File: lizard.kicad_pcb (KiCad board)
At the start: 2 copper layers, 14.8 x 56.2 mm, 13 parts, among them P1 SW DBG, U1 EFM8BB1

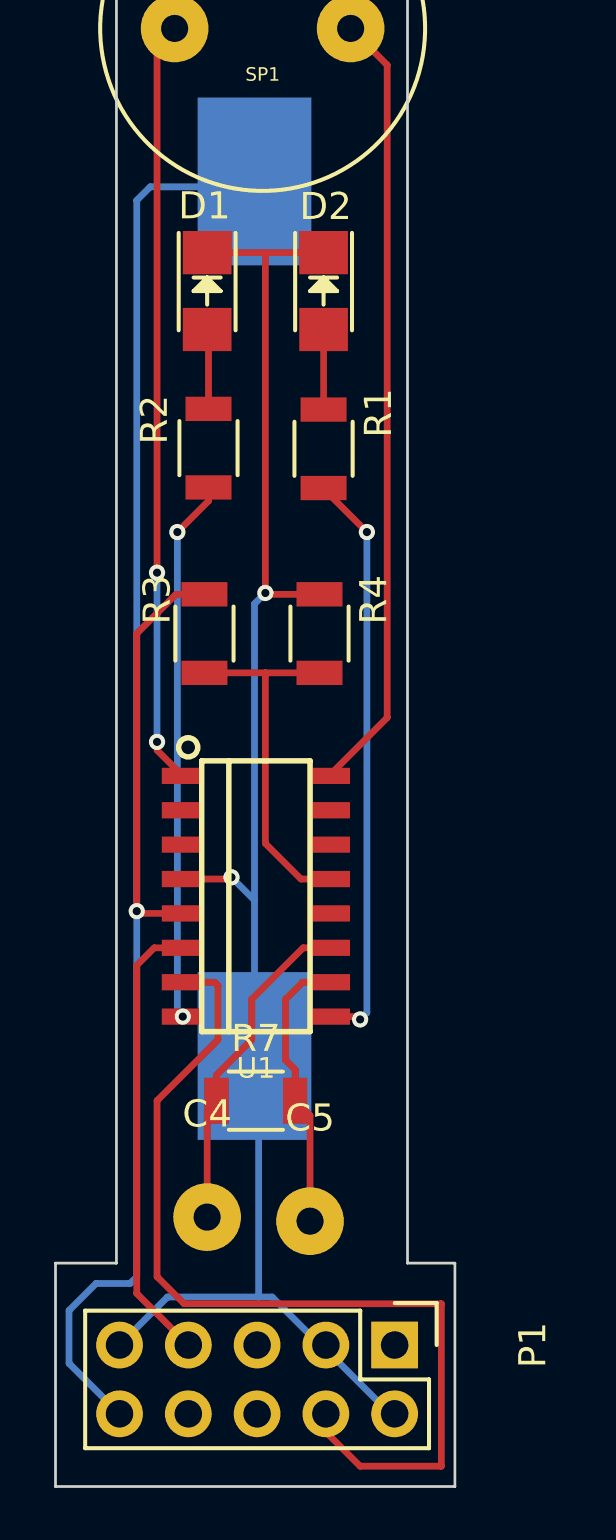
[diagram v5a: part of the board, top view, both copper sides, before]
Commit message: fixed LED resistor values; fixed silk values; misc fixes
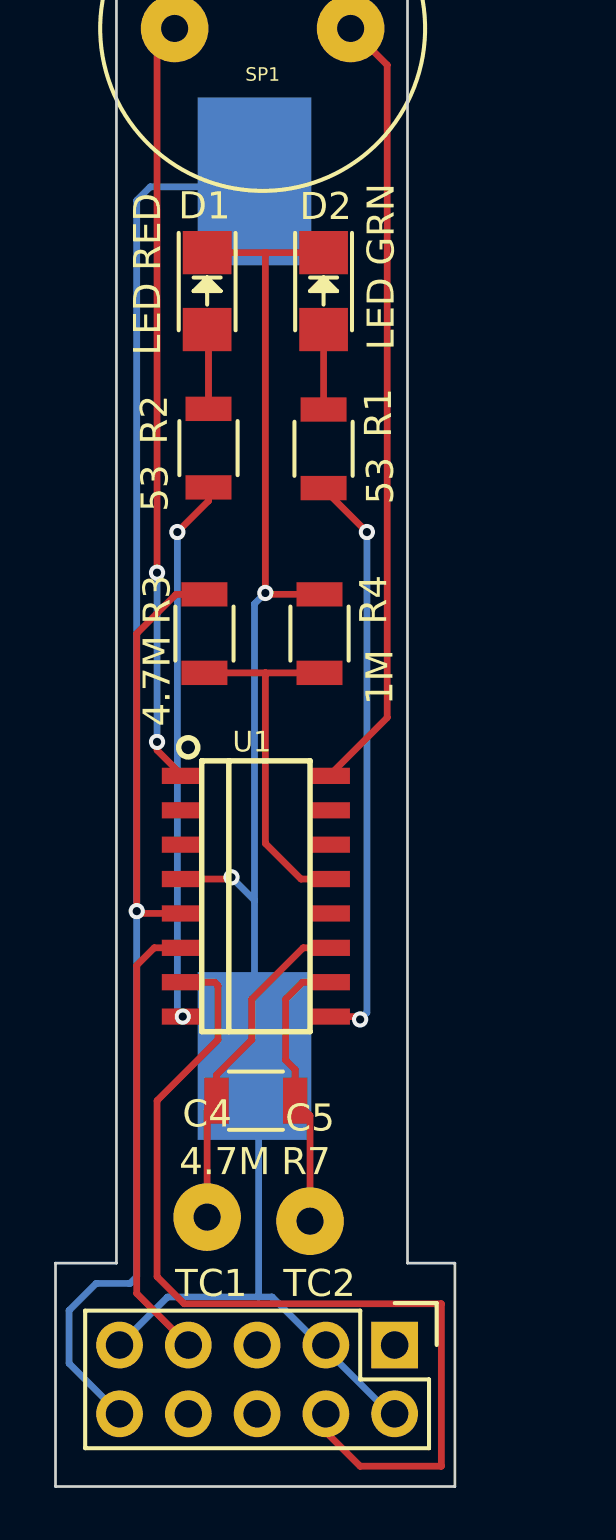
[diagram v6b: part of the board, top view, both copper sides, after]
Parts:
- R1, R2: value 20 -> 53
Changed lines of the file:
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@@
-(kicad_pcb (version 4) (host pcbnew "(2015-06-09 BZR 5726)-product")
+(kicad_pcb (version 4) (host pcbnew "(2015-08-06 BZR 6058)-product")
   (general
     (links 24)
@@
       (effects (font (size 1 1) (thickness 0.15)))
     )
-    (fp_text value TC1 (at -1.905 3.175) (layer F.Fab)
+    (fp_text value TC1 (at 0.15 2.45) (layer F.SilkS)
       (effects (font (size 1 1) (thickness 0.15)))
     )
@@
       (effects (font (size 1 1) (thickness 0.15)))
     )
-    (fp_text value TC2 (at -1.905 3.175) (layer F.Fab)
+    (fp_text value TC2 (at 0.35 2.3) (layer F.SilkS)
       (effects (font (size 1 1) (thickness 0.15)))
     )
@@
       (effects (font (size 1 1) (thickness 0.15)))
     )
-    (fp_text value "LED RED" (at -0.625 2.2 270) (layer F.Fab)
+    (fp_text value "LED RED" (at -0.625 2.2 270) (layer F.SilkS)
       (effects (font (size 1 1) (thickness 0.15)))
     )
@@
       (effects (font (size 1 1) (thickness 0.15)))
     )
-    (fp_text value "LED GRN" (at -0.9 -2.125 270) (layer F.Fab)
+    (fp_text value "LED GRN" (at -0.9 -2.125 270) (layer F.SilkS)
       (effects (font (size 1 1) (thickness 0.15)))
     )
@@
     (descr "Through hole pin header")
     (tags "pin header")
-    (fp_text reference P1 (at 0 -5.1 270) (layer F.SilkS)
-      (effects (font (size 1 1) (thickness 0.15)))
-    )
-    (fp_text value "SW DBG" (at 0 -3.1 270) (layer F.Fab)
+    (fp_text reference P1 (at 0 -5.1 270) (layer F.SilkS) hide
+      (effects (font (size 1 1) (thickness 0.15)))
+    )
+    (fp_text value "SW DBG" (at 0 -3.1 270) (layer F.SilkS) hide
       (effects (font (size 1 1) (thickness 0.15)))
     )
@@
       (effects (font (size 1 1) (thickness 0.15)))
     )
-    (fp_text value 20 (at 1.175 -2.1 270) (layer F.Fab)
+    (fp_text value 53 (at 1.175 -2.1 270) (layer F.SilkS)
       (effects (font (size 1 1) (thickness 0.15)))
     )
@@
       (effects (font (size 1 1) (thickness 0.15)))
     )
-    (fp_text value 20 (at 1.475 1.975 270) (layer F.Fab)
+    (fp_text value 53 (at 1.475 1.975 270) (layer F.SilkS)
       (effects (font (size 1 1) (thickness 0.15)))
     )
@@
       (effects (font (size 1 1) (thickness 0.15)))
     )
-    (fp_text value 4.7M (at 1.75 1.75 270) (layer F.Fab)
+    (fp_text value 4.7M (at 1.75 1.75 270) (layer F.SilkS)
       (effects (font (size 1 1) (thickness 0.15)))
     )
@@
       (effects (font (size 1 1) (thickness 0.15)))
     )
-    (fp_text value 1M (at -0.75 2 90) (layer F.Fab)
+    (fp_text value 1M (at -1.61 2.23 90) (layer F.SilkS)
       (effects (font (size 1 1) (thickness 0.15)))
     )
@@
     (tags "resistor 1206")
     (attr smd)
-    (fp_text reference R7 (at 0 -2.3) (layer F.SilkS)
-      (effects (font (size 1 1) (thickness 0.15)))
-    )
-    (fp_text value 4.7M (at 0 2.3) (layer F.Fab)
+    (fp_text reference R7 (at 1.85 2.25) (layer F.SilkS)
+      (effects (font (size 1 1) (thickness 0.15)))
+    )
+    (fp_text value 4.7M (at -1.15 2.25) (layer F.SilkS)
       (effects (font (size 1 1) (thickness 0.15)))
     )
@@
     (solder_paste_margin -0.0508)
     (attr smd)
-    (fp_text reference U1 (at 0 6.35) (layer F.SilkS)
+    (fp_text reference U1 (at -0.15 -5.7) (layer F.SilkS)
       (effects (font (size 0.762 0.762) (thickness 0.1524)))
     )

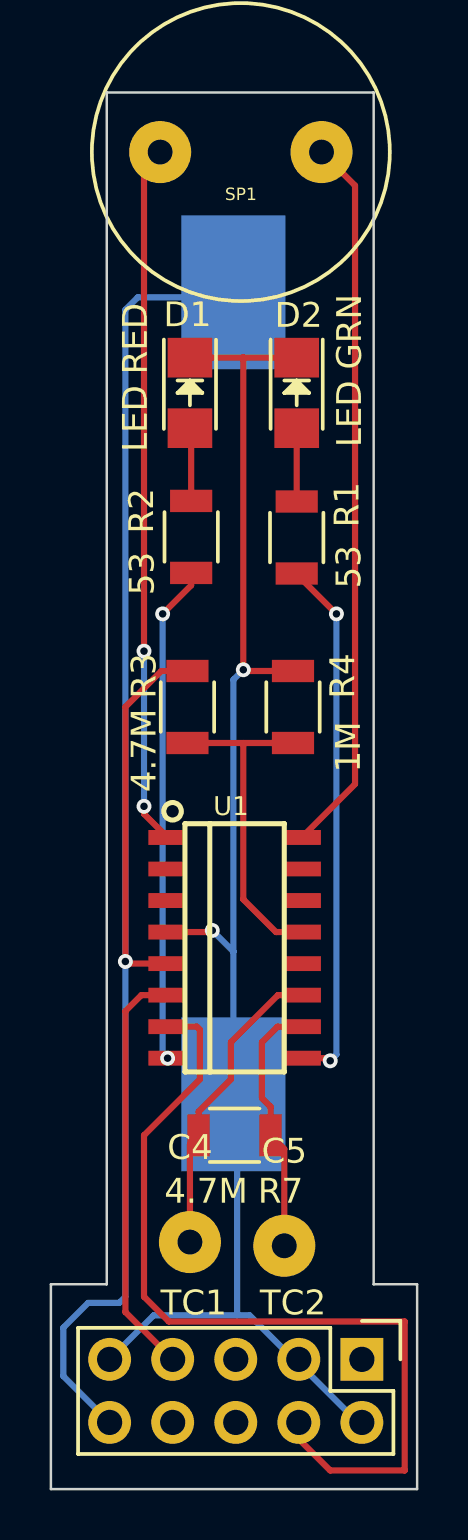
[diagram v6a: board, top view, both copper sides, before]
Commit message: fixed LED resistor values; removed voltage divider; cleaned up layout
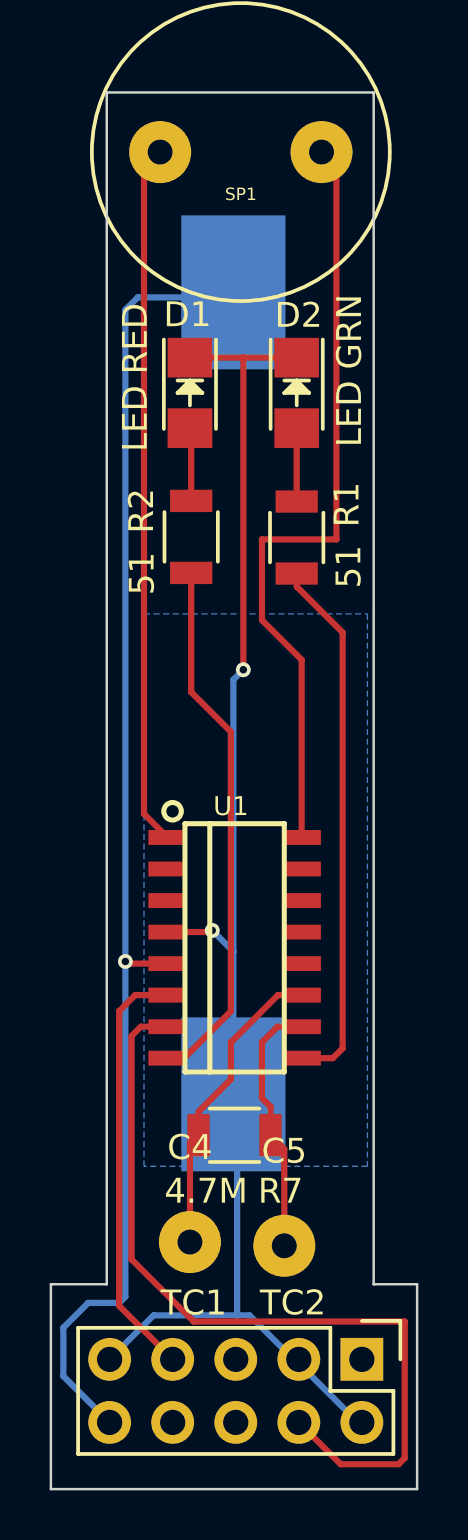
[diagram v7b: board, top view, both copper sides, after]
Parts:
- removed R3: 4.7M, Resistors_SMD:R_1206
- removed R4: 1M, Resistors_SMD:R_1206
- R1, R2: value 53 -> 51
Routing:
- net Net-(U1-Pad13): track 13.4 -> 0.00 mm
- net VDD: track 67.1 -> 53.7 mm
- net Net-(SP1-Pad1): track 29.1 -> 31.5 mm
- net GND: track 61.3 -> 59.3 mm
- net Net-(R2-Pad2): track 20.1 -> 21.6 mm, vias 2 -> 0
- net Net-(P1-Pad4): track 35.4 -> 33.9 mm
- net Net-(R1-Pad2): track 21.6 -> 21.7 mm, vias 2 -> 0
- net Net-(SP1-Pad2): vias 2 -> 0
- added copper zone on B.Cu, net GND
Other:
- board text added: "1.0b"
- board text added: "Desert Lizard Board v1.0b Copyright © 2015 Bart Massey http://github.com/DesertLizard/LizardBoard"
- board text removed: "1.0"
- board text removed: "Desert Lizard Board v1.0 Copyright © 2015 Bart Massey http://github.com/DesertLizard/LizardBoard"

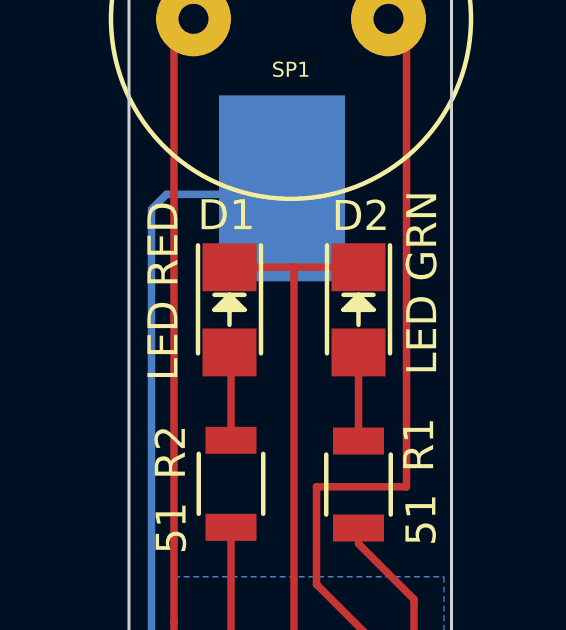
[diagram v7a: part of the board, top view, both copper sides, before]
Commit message: added + and C for diodes
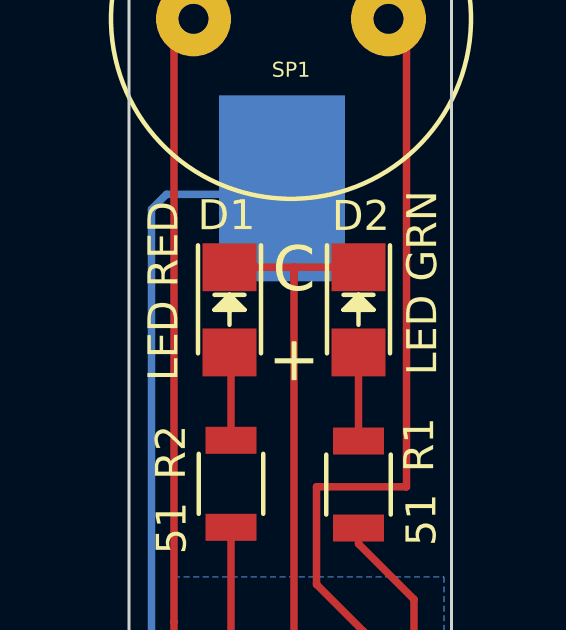
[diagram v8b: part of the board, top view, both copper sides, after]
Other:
- board text added: "+"
- board text added: "C"
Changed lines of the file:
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@@
-(kicad_pcb (version 4) (host pcbnew "(2015-06-09 BZR 5726)-product")
+(kicad_pcb (version 4) (host pcbnew "(2015-08-06 BZR 6058)-product")
   (general
     (links 20)
     (no_connects 0)
-    (area 113.699999 91.699999 128.550001 148.050001)
+    (area 109.574999 87.874999 256.578571 200.3)
     (thickness 1.6)
-    (drawings 14)
+    (drawings 16)
     (tracks 89)
     (zones 0)
@@
       (net 16 "Net-(SP1-Pad1)"))
   )
+  (gr_text C (at 121.5 102.5) (layer F.SilkS)
+    (effects (font (size 1.5 1.5) (thickness 0.3)))
+  )
+  (gr_text + (at 121.5 105.5) (layer F.SilkS)
+    (effects (font (size 1.5 1.5) (thickness 0.3)))
+  )
   (gr_line (start 126.75 91.75) (end 116 91.75) (angle 90) (layer Edge.Cuts) (width 0.1))
